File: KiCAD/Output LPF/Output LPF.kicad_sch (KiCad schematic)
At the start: 83 parts, among them J16 Screw_Terminal_01x02, J25 Screw_Terminal_01x02, J26 Screw_Terminal_01x02, J27 Screw_Terminal_01x02, J28 Filter In, K1 Relay_RSS-SR042P, K2 Relay_RSS-SR042P, K3 Relay_RSS-SR042P, K4 Relay_RSS-SR042P, Q1 2N7000, Q5 2N7000, Q8 2N7000, Q9 2N7000, U3 LM7171xIN

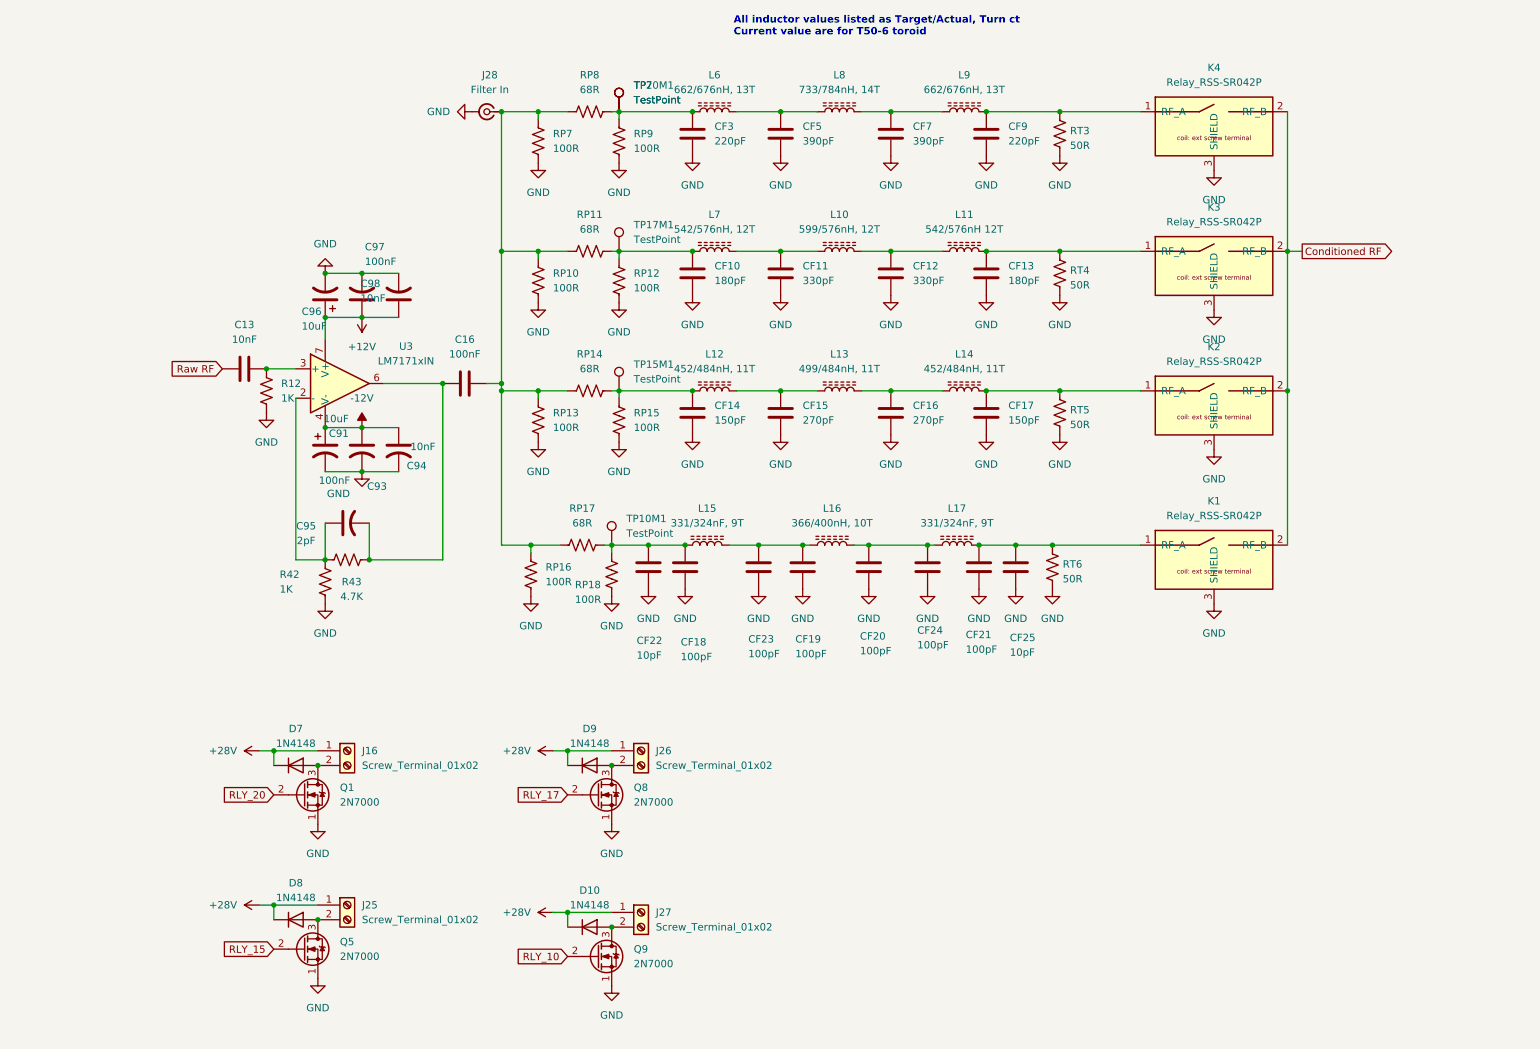
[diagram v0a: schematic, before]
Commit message: revD: Output LPF banks 1-2 pi-pad topology, +28V umbilical from analog
- Output LPF (K5/K6 banks): shared input pi-pad on common rail (R1 100R
  shunt + R2 68R series) feeds the band-select fanout; per-bank
  post-relay shunt (RP9, RP12) at each LPF input to dissipate residual
  bank-to-bank leakage. Banks 3-4 (K1/K2/K7/K8) still pending.
- Output LPF: coil-driver chain for 5 band relays (2N7000 Q1/Q5/Q8-10
  + 1N4148 flyback D7-D11 + screw terminals J16/J25/J26/J27/J29 with
  pin 1=+28V, pin 2=FET drain).
- Analog J2 RJ45 to LPF: pin 8=+28V, pins 6/7/SH=GND, pins 1-5=
  RLY_10/15/17/20/40. Netlist regenerated; +28V and all 5 RLY_xx
  signals resolve on both sides.
- Output LPF project: add sym-lib-table and fp-lib-table pointing at
  ../xmitter.kicad_sym and ../xmitter.pretty (mirrors ss_pa/analog
  convention).

Co-Authored-By: Claude Opus 4.7 <noreply@anthropic.com>
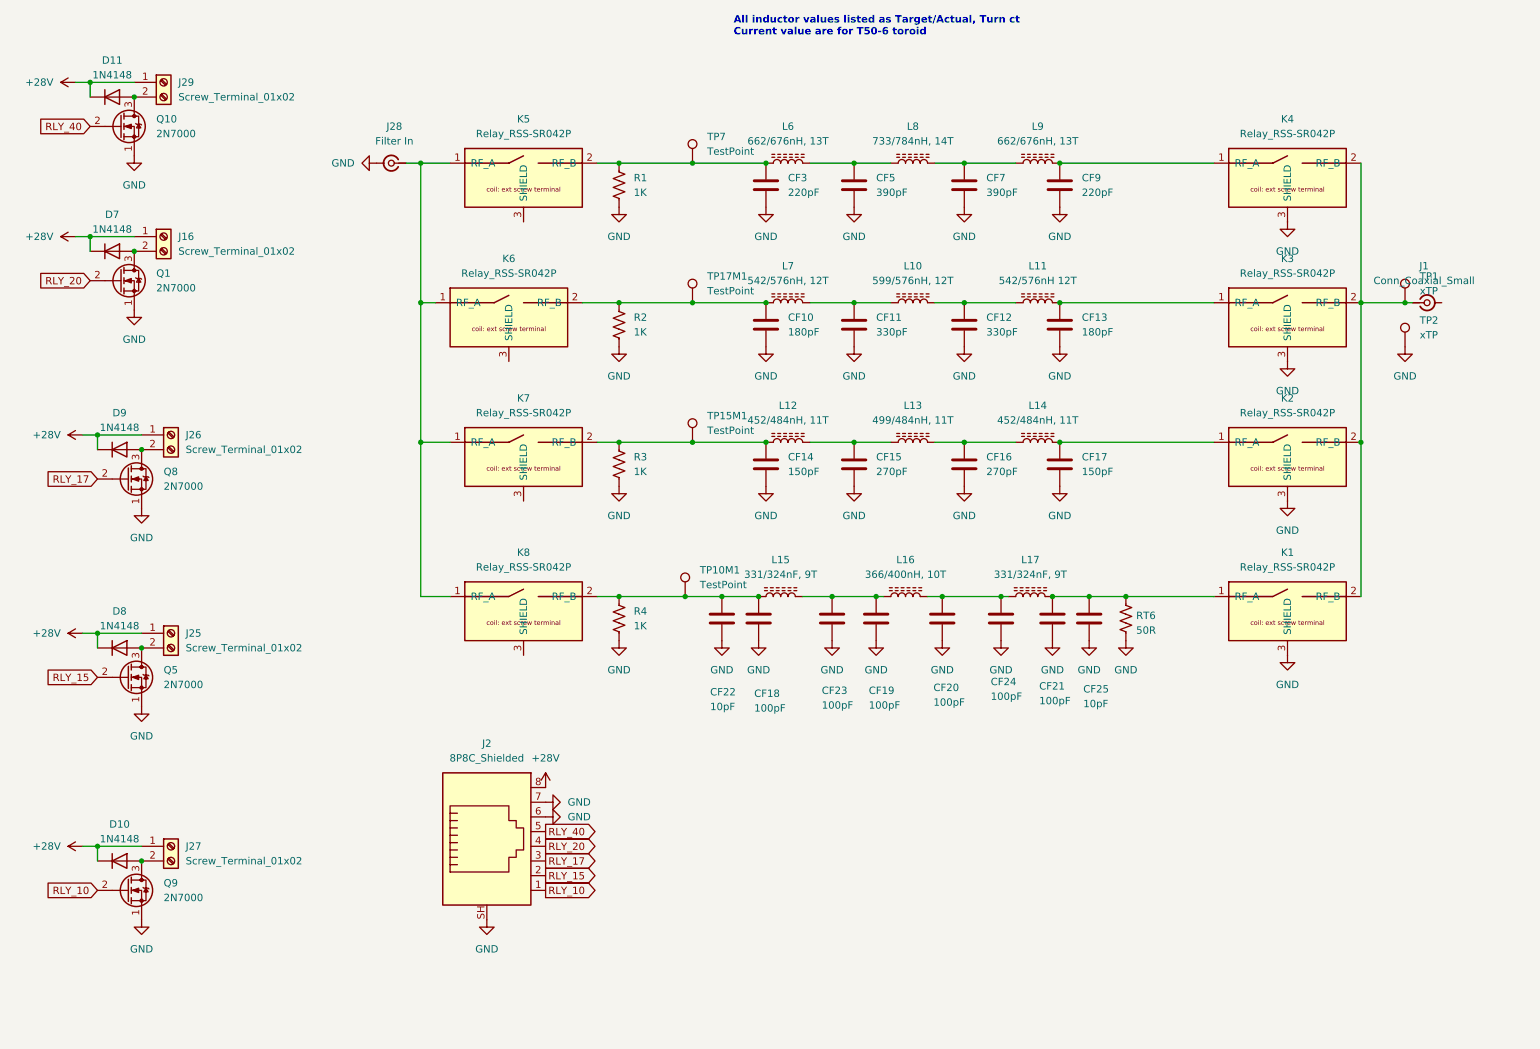
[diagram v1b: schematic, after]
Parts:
- removed C13: 10nF, Capacitor_THT:C_Disc_D6.0mm_W2.5mm_P5.00mm, symbol Device:C
- removed C16: 100nF, Capacitor_THT:C_Disc_D5.0mm_W2.5mm_P5.00mm, symbol Device:C
- removed C91, C96: 10uF, Capacitor_THT:CP_Radial_D5.0mm_P2.00mm, symbol Device:C_Polarized_US
- removed C93, C97: 100nF, Capacitor_THT:C_Disc_D5.0mm_W2.5mm_P5.00mm, symbol Device:C_US
- removed C94, C98: 10nF, Capacitor_THT:C_Disc_D6.0mm_W2.5mm_P5.00mm, symbol Device:C_US
- removed C95: 2pF, xmitter:C_Axial_Kemet_Aximax_C41X_L4.5mm_D2.6mm_P7.62mm_Horizontal, symbol Device:C_US
- removed R12, R42: 1K, Resistor_THT:R_Axial_DIN0207_L6.3mm_D2.5mm_P10.16mm_Horizontal, symbol Device:R_US
- removed R43: 4.7K, Resistor_THT:R_Axial_DIN0207_L6.3mm_D2.5mm_P10.16mm_Horizontal, symbol Device:R_US
- removed RP10, RP12, RP13, RP15, RP16, RP18, RP7, RP9: 100R, Resistor_THT:R_Axial_DIN0207_L6.3mm_D2.5mm_P10.16mm_Horizontal, symbol Device:R_US
- removed RP11, RP14, RP17, RP8: 68R, Resistor_THT:R_Axial_DIN0207_L6.3mm_D2.5mm_P10.16mm_Horizontal, symbol Device:R_US
- removed RT3, RT4, RT5: 50R, Resistor_THT:R_Axial_DIN0207_L6.3mm_D2.5mm_P10.16mm_Horizontal, symbol Device:R_US
- removed TP20M1: TestPoint, Connector_PinHeader_2.54mm:PinHeader_1x01_P2.54mm_Vertical, symbol Connector:TestPoint
- removed U3: LM7171xIN, Package_DIP:DIP-8_W7.62mm, symbol Amplifier_Operational:LM7171xIN
- added D11: 1N4148, Diode_THT:D_DO-35_SOD27_P7.62mm_Horizontal, symbol Diode:1N4148
- added J1: Conn_Coaxial_Small, symbol Connector:Conn_Coaxial_Small
- added J2: 8P8C_Shielded, xmitter:Amphenol_RJE1D-188_Horizontal_Shielded, symbol Connector:8P8C_Shielded
- added J29: Screw_Terminal_01x02, TerminalBlock_Phoenix:TerminalBlock_Phoenix_MKDS-1,5-2_1x02_P5.00mm_Horizontal, symbol Connector:Screw_Terminal_01x02
- added K5, K6, K7, K8: Relay_RSS-SR042P, xmitter:Relay_SPST_RelComm_RSS-SR042P, symbol xmitter:Relay_SPST_RSS-SR042P
- added Q10: 2N7000, Package_TO_SOT_THT:TO-92_Inline, symbol Transistor_FET:2N7000
- added R1, R2, R3, R4: 1K, symbol Device:R_US
- added TP1, TP2: xTP, Connector_PinHeader_2.54mm:PinHeader_1x01_P2.54mm_Vertical, symbol xmitter:xTP
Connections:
- net +28V: now also D11.1 (K), J2.8, J29.1 (Pin_1)
- net GND: now also J2.6, J2.7, J2.SH, Q10.1 (S), R1.2, R2.2, R3.2, R4.2, TP2.1
- net RLY_10: now also J2.1
- net RLY_15: now also J2.2
- net RLY_17: now also J2.3
- net RLY_20: now also J2.4
- net at J28.1 (In): now also K5.1 (RF_A), K6.1 (RF_A), K7.1 (RF_A), K8.1 (RF_A)
- net at CF14.1, L12.1, TP15M1.1: now also K7.2 (RF_B), R3.1
- net at CF3.1, L6.1, TP7.1: now also K5.2 (RF_B), R1.1
- net at CF10.1, L7.1, TP17M1.1: now also K6.2 (RF_B), R2.1
- net at CF18.1, CF22.1, L15.1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: now also K8.2 (RF_B), R4.1
- net Conditioned RF: no longer names the net of K1.2 (RF_B), K2.2 (RF_B), K3.2 (RF_B), K4.2 (RF_B)
- net Conditioned RF: now also J1.1 (In), TP1.1
- new net: D11.2 (A), J29.2 (Pin_2), Q10.3 (D)
- new net RLY_40: J2.5, Q10.2 (G)
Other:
- moved on the sheet: CF10, CF11, CF12, CF13, CF14, CF15, CF16, CF17, CF18, CF19, CF20, CF21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

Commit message: revD Output LPF: 5-band buildout (40m/20m/17m/15m/10m)
Safety point before hierarchical refactor for layout replication.

- 5 LPF banks drawn: K9=40m, K5=20m, K6=17m, K7=15m, K8=10m
- 7-pole 0.1 dB Chebyshev at 50 Ohm; outer+center series inductors
  on same core (A_L = 4.0 nH/N^2) + pi shunt caps per bank
- 20m/17m/15m/10m: values confirmed against Chebyshev tables
- 40m: pending fix (currently a copy of 20m values); target
  fc=8 MHz with L_outer=19T/1444nH, L_center=20T/1600nH,
  C_outer=470pF, C_center=820pF
- 10m: L15/L17 value fields still say "nF" (typo, should be "nH")

Co-Authored-By: Claude Opus 4.7 <noreply@anthropic.com>
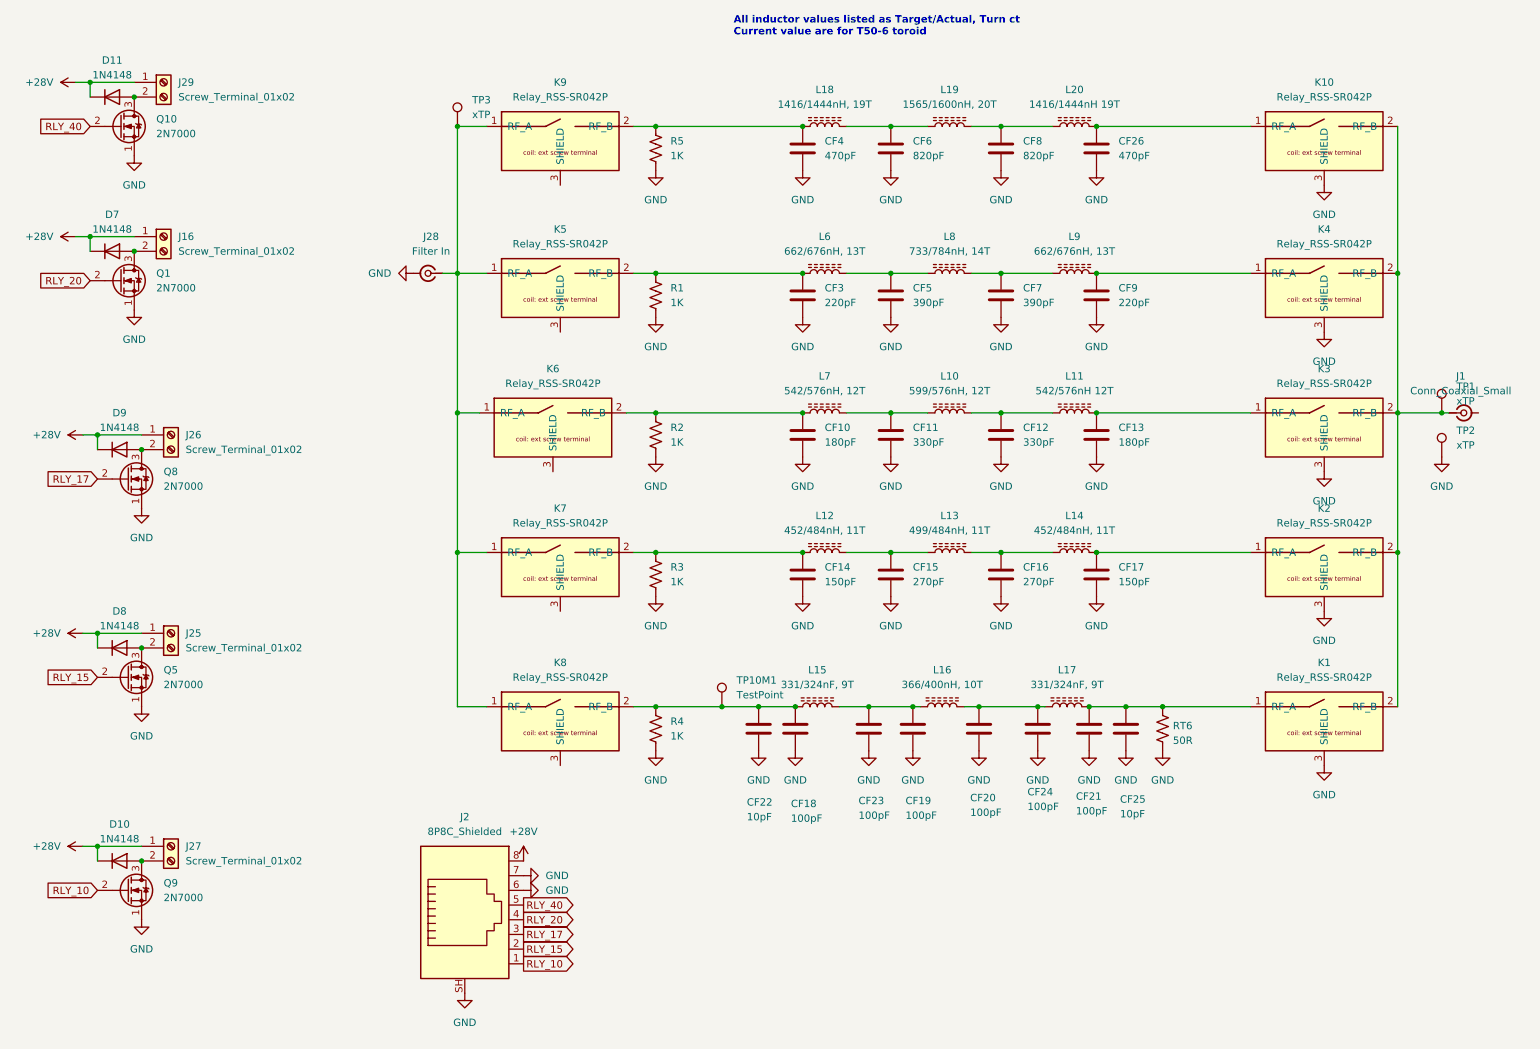
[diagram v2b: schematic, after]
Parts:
- removed TP15M1, TP17M1, TP7: TestPoint, Connector_PinHeader_2.54mm:PinHeader_1x01_P2.54mm_Vertical, symbol Connector:TestPoint
- added CF26, CF4: 470pF, Capacitor_THT:C_Disc_D6.0mm_W2.5mm_P5.00mm, symbol Device:C
- added CF6, CF8: 820pF, Capacitor_THT:C_Disc_D7.5mm_W2.5mm_P5.00mm, symbol Device:C
- added K10, K9: Relay_RSS-SR042P, xmitter:Relay_SPST_RelComm_RSS-SR042P, symbol xmitter:Relay_SPST_RSS-SR042P
- added L18: 1416/1444nH, 19T, xmitter:T50-6_Vertical_HandWound, symbol Device:L_Ferrite
- added L19: 1565/1600nH, 20T, xmitter:T50-6_Flat_HandWound, symbol Device:L_Ferrite
- added L20: 1416/1444nH 19T, xmitter:T50-6_Vertical_HandWound, symbol Device:L_Ferrite
- added R5: 1K, symbol Device:R_US
- added TP3: xTP, Connector_PinHeader_2.54mm:PinHeader_1x01_P2.54mm_Vertical, symbol xmitter:xTP
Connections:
- net GND: now also CF26.2, CF4.2, CF6.2, CF8.2, K10.3 (SHIELD), R5.2
- net at J1.1 (In), K1.2 (RF_B), K2.2 (RF_B)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: now also K10.2 (RF_B)
- net at J28.1 (In), K5.1 (RF_A), K6.1 (RF_A)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: now also K9.1 (RF_A), TP3.1
- new net: CF8.1, L19.2, L20.1
- new net: CF4.1, K9.2 (RF_B), L18.1, R5.1
- new net: CF26.1, K10.1 (RF_A), L20.2
- new net: CF6.1, L18.2, L19.1
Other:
- moved on the sheet: CF10, CF11, CF12, CF13, CF14, CF15, CF16, CF17, CF18, CF19, CF20, CF21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

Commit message: revD Output LPF: R1-R5 footprints + fix missing GNDs
- Assign R_Axial_DIN0207 horizontal 1/4W footprint to R1-R5
  (1 kOhm per-bank input swamp resistors on K5/K6/K7/K8/K9)
- Fix missing GND connections on shunt caps / returns

Co-Authored-By: Claude Opus 4.7 <noreply@anthropic.com>
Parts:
- R1, R2, R3, R4, R5: footprint (none) -> Resistor_THT:R_Axial_DIN0207_L6.3mm_D2.5mm_P10.16mm_Horizontal
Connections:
- net GND: now also J1.2 (Ext), K5.3 (SHIELD), K6.3 (SHIELD), K7.3 (SHIELD), K8.3 (SHIELD), K9.3 (SHIELD)

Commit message: revD Output LPF: regenerate netlist, project settings touch-up
Checkpoint before revisiting board layout -- the RSS-SR042P relays
dominate the current board area and the relay choice may change.

Co-Authored-By: Claude Opus 4.7 <noreply@anthropic.com>
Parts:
- J1: footprint (none) -> Connector_Coaxial:SMA_Amphenol_132134_Vertical
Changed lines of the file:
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@@
 			)
 		)
-		(property "Footprint" ""
+		(property "Footprint" "Connector_Coaxial:SMA_Amphenol_132134_Vertical"
 			(at 266.7 83.82 0)
 			(hide yes)
